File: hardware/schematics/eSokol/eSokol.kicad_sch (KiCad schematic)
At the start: 0 parts

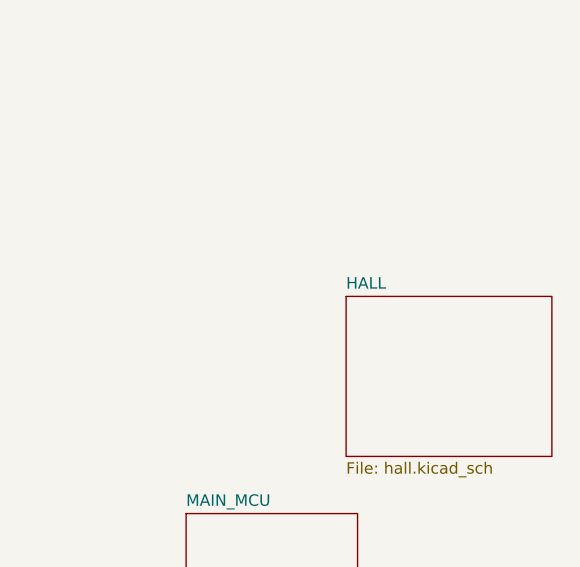
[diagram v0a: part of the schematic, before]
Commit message: hardware: schematics: Fix improper NMOS placement, misc minor fixes
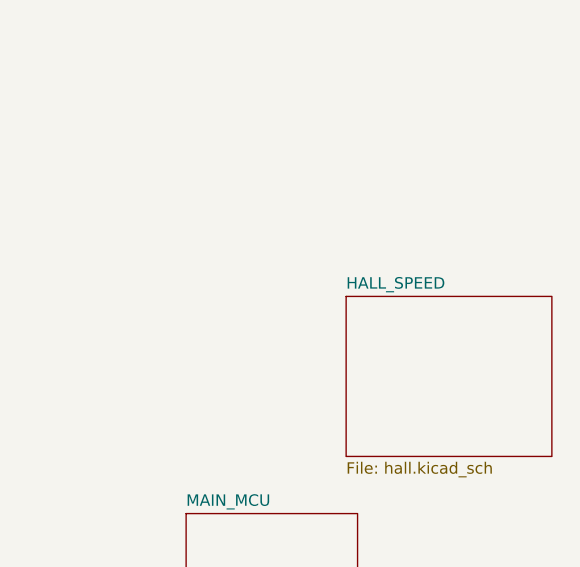
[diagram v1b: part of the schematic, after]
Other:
- sheet HALL renamed HALL_SPEED
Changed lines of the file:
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@@
 			(color 0 0 0 0.0000)
 		)
-		(property "Sheetname" "HALL"
+		(property "Sheetname" "HALL_SPEED"
 			(at 212.09 60.2484 0)
 			(effects

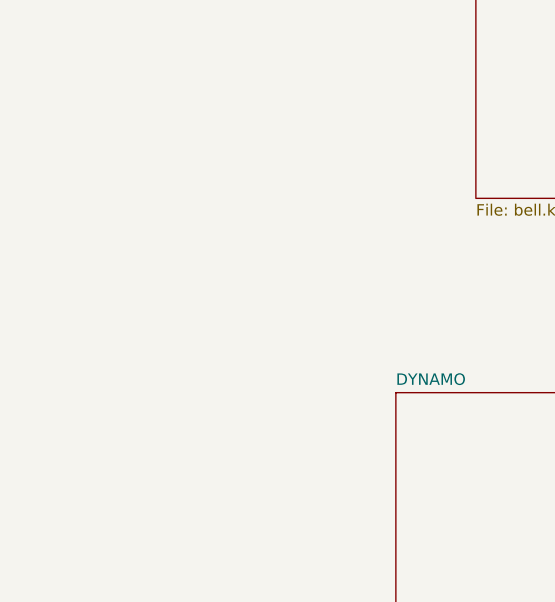
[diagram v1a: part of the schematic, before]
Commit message: Fix throttle transistor layout once more, move throttle to a separate page. Still needs testing.
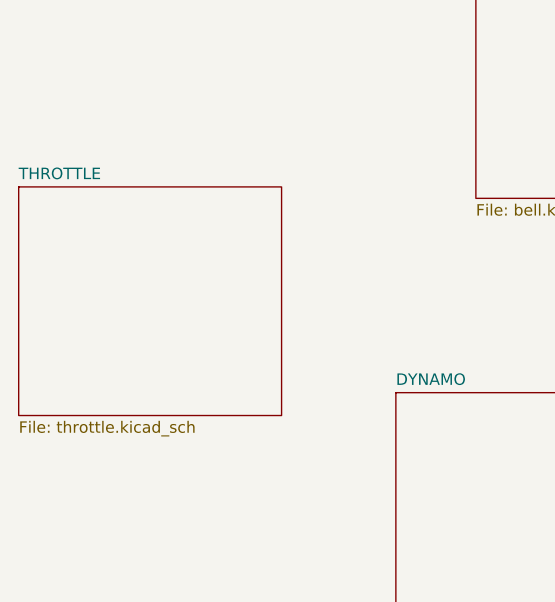
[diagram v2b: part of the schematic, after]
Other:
- added sheet THROTTLE (throttle.kicad_sch)
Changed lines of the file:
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@@
 	(paper "A4")
+	(sheet
+		(at 33.02 53.34)
+		(size 29.21 25.4)
+		(fields_autoplaced yes)
+		(stroke
+			(width 0.1524)
+			(type solid)
+		)
+		(fill
+			(color 0 0 0 0.0000)
+		)
+		(property "Sheetname" "THROTTLE"
+			(at 33.02 52.6284 0)
+			(effects
+				(font
+					(size 1.27 1.27)
+				)
+				(justify left bottom)
+			)
+		)
+		(property "Sheetfile" "throttle.kicad_sch"
+			(at 33.02 79.3246 0)
+			(effects
+				(font
+					(size 1.27 1.27)
+				)
+				(justify left top)
+			)
+		)
+		(instances
+			(project "eSokol"
+				(path "/44b9e6ec-08e4-4361-b4b8-e7c9cf0a26a7"
+					(page "10")
+				)
+			)
+		)
+	)
 	(sheet
 		(at 185.42 107.95)

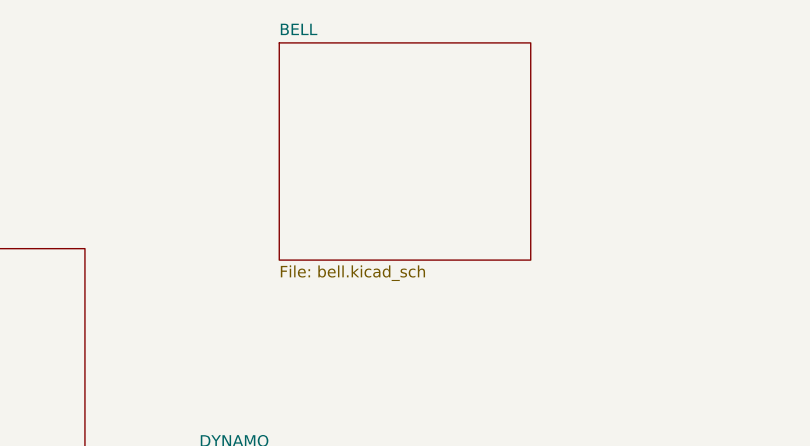
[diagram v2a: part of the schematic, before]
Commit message: schematics: (almost) finalize throttle circuit (it's working :D), minor cleanups
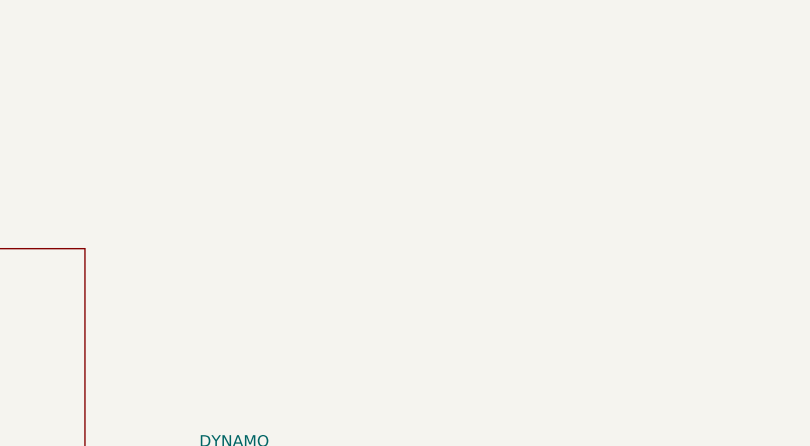
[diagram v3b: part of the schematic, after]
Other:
- removed sheet BELL
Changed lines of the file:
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@@
-	)
-	(sheet
-		(at 83.82 30.48)
-		(size 27.94 24.13)
-		(fields_autoplaced yes)
-		(stroke
-			(width 0.1524)
-			(type solid)
-		)
-		(fill
-			(color 0 0 0 0.0000)
-		)
-		(property "Sheetname" "BELL"
-			(at 83.82 29.7684 0)
-			(show_name yes)
-			(effects
-				(font
-					(size 1.27 1.27)
-				)
-				(justify left bottom)
-			)
-		)
-		(property "Sheetfile" "bell.kicad_sch"
-			(at 83.82 55.1946 0)
-			(effects
-				(font
-					(size 1.27 1.27)
-				)
-				(justify left top)
-			)
-		)
-		(instances
-			(project "eSokol"
-				(path "/44b9e6ec-08e4-4361-b4b8-e7c9cf0a26a7"
-					(page "9")
-				)
-			)
-		)
 	)
 	(sheet

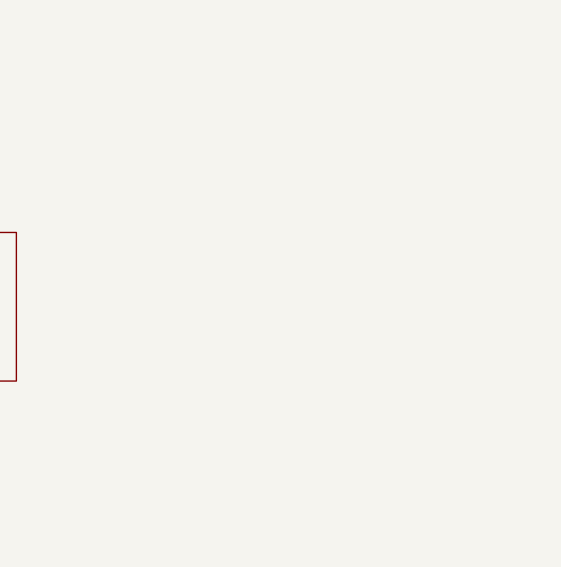
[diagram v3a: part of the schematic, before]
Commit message: Update throttle circuits, move bigbatt to its own sheet and design ds-vc288 circuit
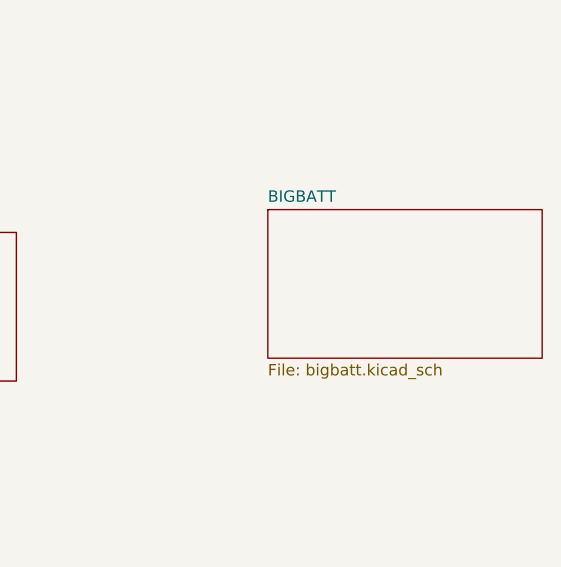
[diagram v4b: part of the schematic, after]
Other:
- added sheet BIGBATT (bigbatt.kicad_sch)
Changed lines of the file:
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@@
+	)
+	(sheet
+		(at 245.11 105.41)
+		(size 30.48 16.51)
+		(fields_autoplaced yes)
+		(stroke
+			(width 0.1524)
+			(type solid)
+		)
+		(fill
+			(color 0 0 0 0.0000)
+		)
+		(property "Sheetname" "BIGBATT"
+			(at 245.11 104.6984 0)
+			(effects
+				(font
+					(size 1.27 1.27)
+				)
+				(justify left bottom)
+			)
+		)
+		(property "Sheetfile" "bigbatt.kicad_sch"
+			(at 245.11 122.5046 0)
+			(effects
+				(font
+					(size 1.27 1.27)
+				)
+				(justify left top)
+			)
+		)
+		(instances
+			(project "eSokol"
+				(path "/44b9e6ec-08e4-4361-b4b8-e7c9cf0a26a7"
+					(page "10")
+				)
+			)
+		)
 	)
 	(sheet

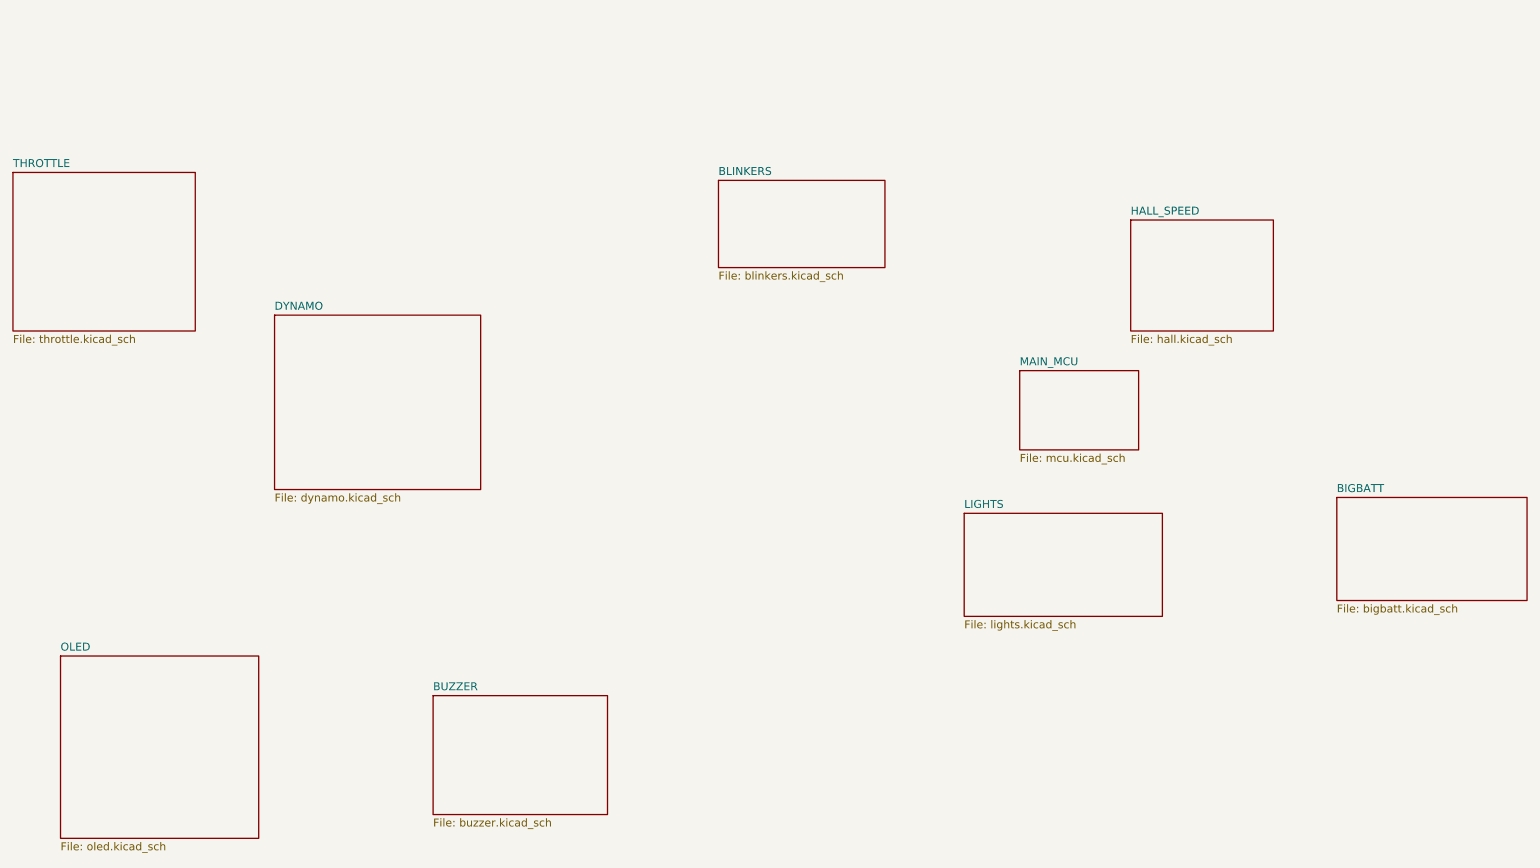
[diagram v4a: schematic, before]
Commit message: Create one BIG schematic containing everything related to motor and its driver
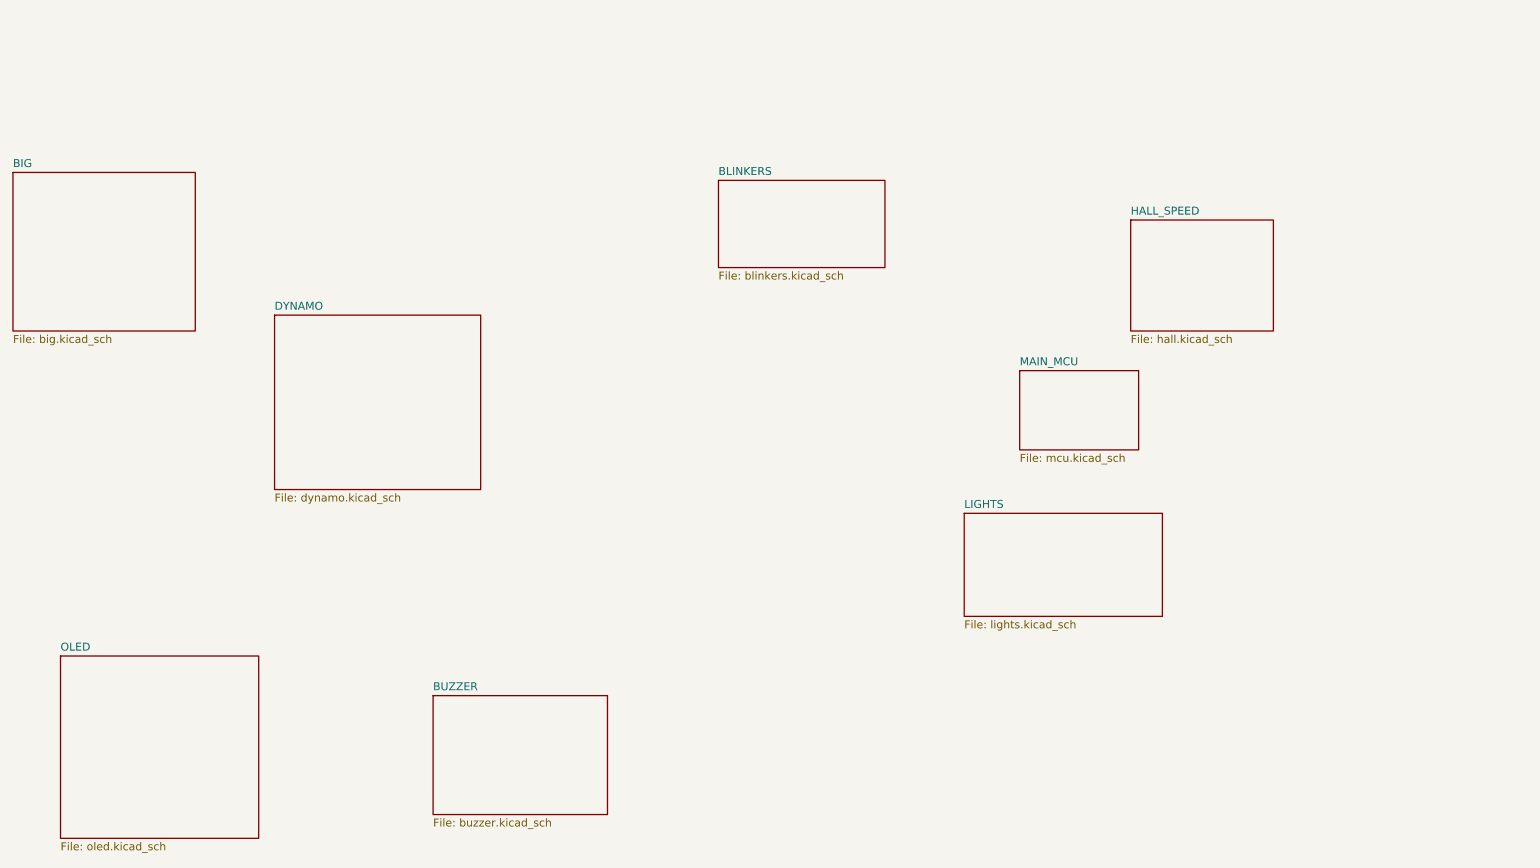
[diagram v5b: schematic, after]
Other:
- sheet THROTTLE renamed BIG
- removed sheet BIGBATT
- sheet BIG: file throttle.kicad_sch -> big.kicad_sch
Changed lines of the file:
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@@
 			(color 0 0 0 0.0000)
 		)
-		(property "Sheetname" "THROTTLE"
+		(property "Sheetname" "BIG"
 			(at 33.02 52.6284 0)
 			(effects
@@
 			)
 		)
-		(property "Sheetfile" "throttle.kicad_sch"
+		(property "Sheetfile" "big.kicad_sch"
 			(at 33.02 79.3246 0)
 			(effects
@@
 				)
 			)
-		)
-	)
-	(sheet
-		(at 245.11 105.41)
-		(size 30.48 16.51)
-		(fields_autoplaced yes)
-		(stroke
-			(width 0.1524)
-			(type solid)
-		)
-		(fill
-			(color 0 0 0 0.0000)
-		)
-		(property "Sheetname" "BIGBATT"
-			(at 245.11 104.6984 0)
-			(effects
-				(font
-					(size 1.27 1.27)
-				)
-				(justify left bottom)
-			)
-		)
-		(property "Sheetfile" "bigbatt.kicad_sch"
-			(at 245.11 122.5046 0)
-			(effects
-				(font
-					(size 1.27 1.27)
-				)
-				(justify left top)
-			)
-		)
-		(instances
-			(project "eSokol"
-				(path "/44b9e6ec-08e4-4361-b4b8-e7c9cf0a26a7"
-					(page "10")
-				)
-			)

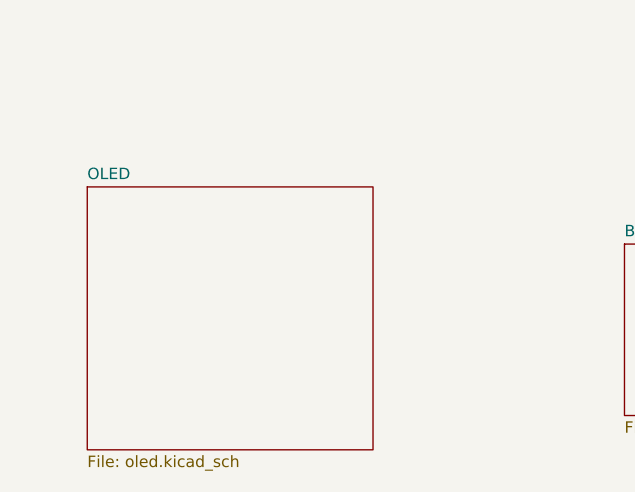
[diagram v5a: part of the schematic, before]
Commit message: hardware/schematics: Replace screen-based control for HC-05 smartphone-app-based control, add buzzer RC filter, rework cold LED circuit
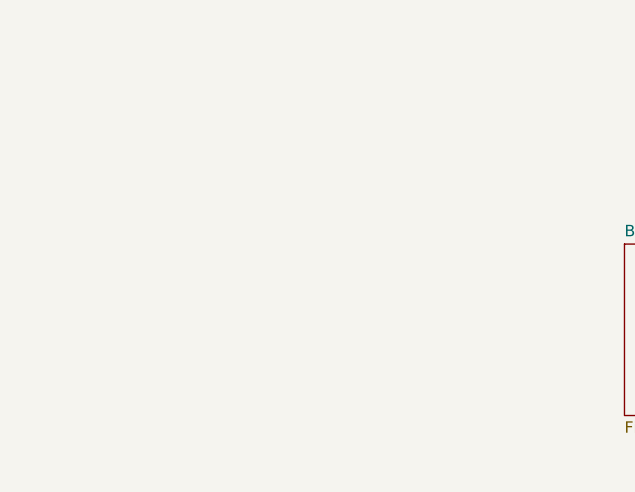
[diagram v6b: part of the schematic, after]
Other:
- removed sheet OLED
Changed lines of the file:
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@@
-	)
-	(sheet
-		(at 40.64 130.81)
-		(size 31.75 29.21)
-		(fields_autoplaced yes)
-		(stroke
-			(width 0.1524)
-			(type solid)
-		)
-		(fill
-			(color 0 0 0 0.0000)
-		)
-		(property "Sheetname" "OLED"
-			(at 40.64 130.0984 0)
-			(effects
-				(font
-					(size 1.27 1.27)
-				)
-				(justify left bottom)
-			)
-		)
-		(property "Sheetfile" "oled.kicad_sch"
-			(at 40.64 160.6046 0)
-			(effects
-				(font
-					(size 1.27 1.27)
-				)
-				(justify left top)
-			)
-		)
-		(property "Pole2" ""
-			(at 40.64 130.81 0)
-			(effects
-				(font
-					(size 1.27 1.27)
-				)
-				(hide yes)
-			)
-		)
-		(instances
-			(project "eSokol"
-				(path "/44b9e6ec-08e4-4361-b4b8-e7c9cf0a26a7"
-					(page "8")
-				)
-			)
-		)
 	)
 	(sheet

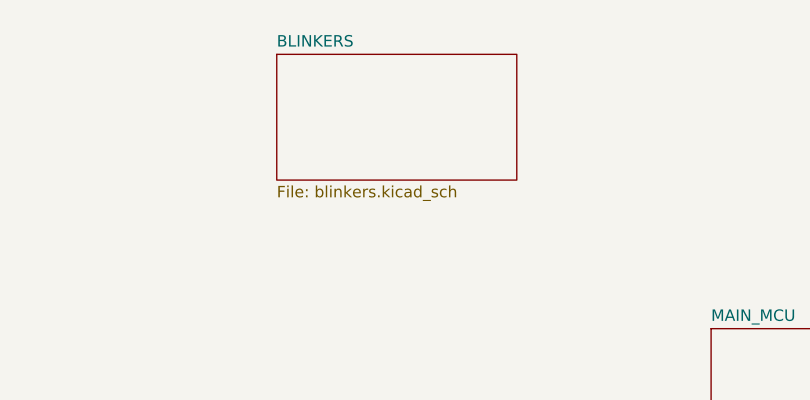
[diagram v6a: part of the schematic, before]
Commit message: hardware/schematics: updated eSokol to reflect new features: ambient light LDR sensor and blinkers Remove old NE555-based blinkers circuit too
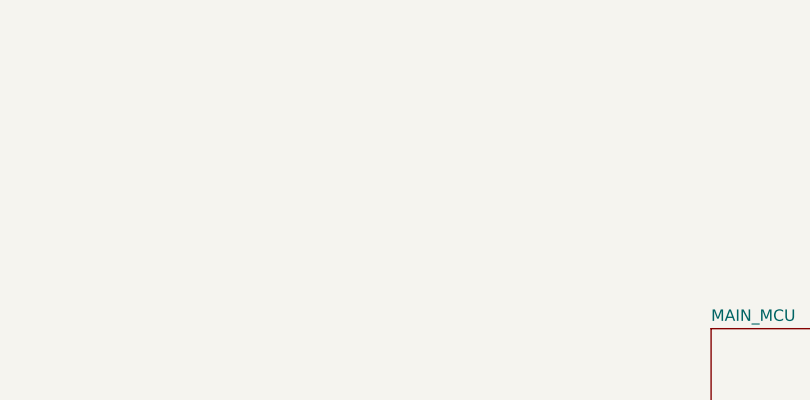
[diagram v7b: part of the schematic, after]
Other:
- removed sheet BLINKERS
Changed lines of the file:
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@@
-	)
-	(sheet
-		(at 146.05 54.61)
-		(size 26.67 13.97)
-		(fields_autoplaced yes)
-		(stroke
-			(width 0.1524)
-			(type solid)
-		)
-		(fill
-			(color 0 0 0 0.0000)
-		)
-		(property "Sheetname" "BLINKERS"
-			(at 146.05 53.8984 0)
-			(effects
-				(font
-					(size 1.27 1.27)
-				)
-				(justify left bottom)
-			)
-		)
-		(property "Sheetfile" "blinkers.kicad_sch"
-			(at 146.05 69.1646 0)
-			(effects
-				(font
-					(size 1.27 1.27)
-				)
-				(justify left top)
-			)
-		)
-		(instances
-			(project "eSokol"
-				(path "/44b9e6ec-08e4-4361-b4b8-e7c9cf0a26a7"
-					(page "9")
-				)
-			)
-		)
 	)
 	(sheet
